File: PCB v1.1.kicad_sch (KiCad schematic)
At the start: 4 parts

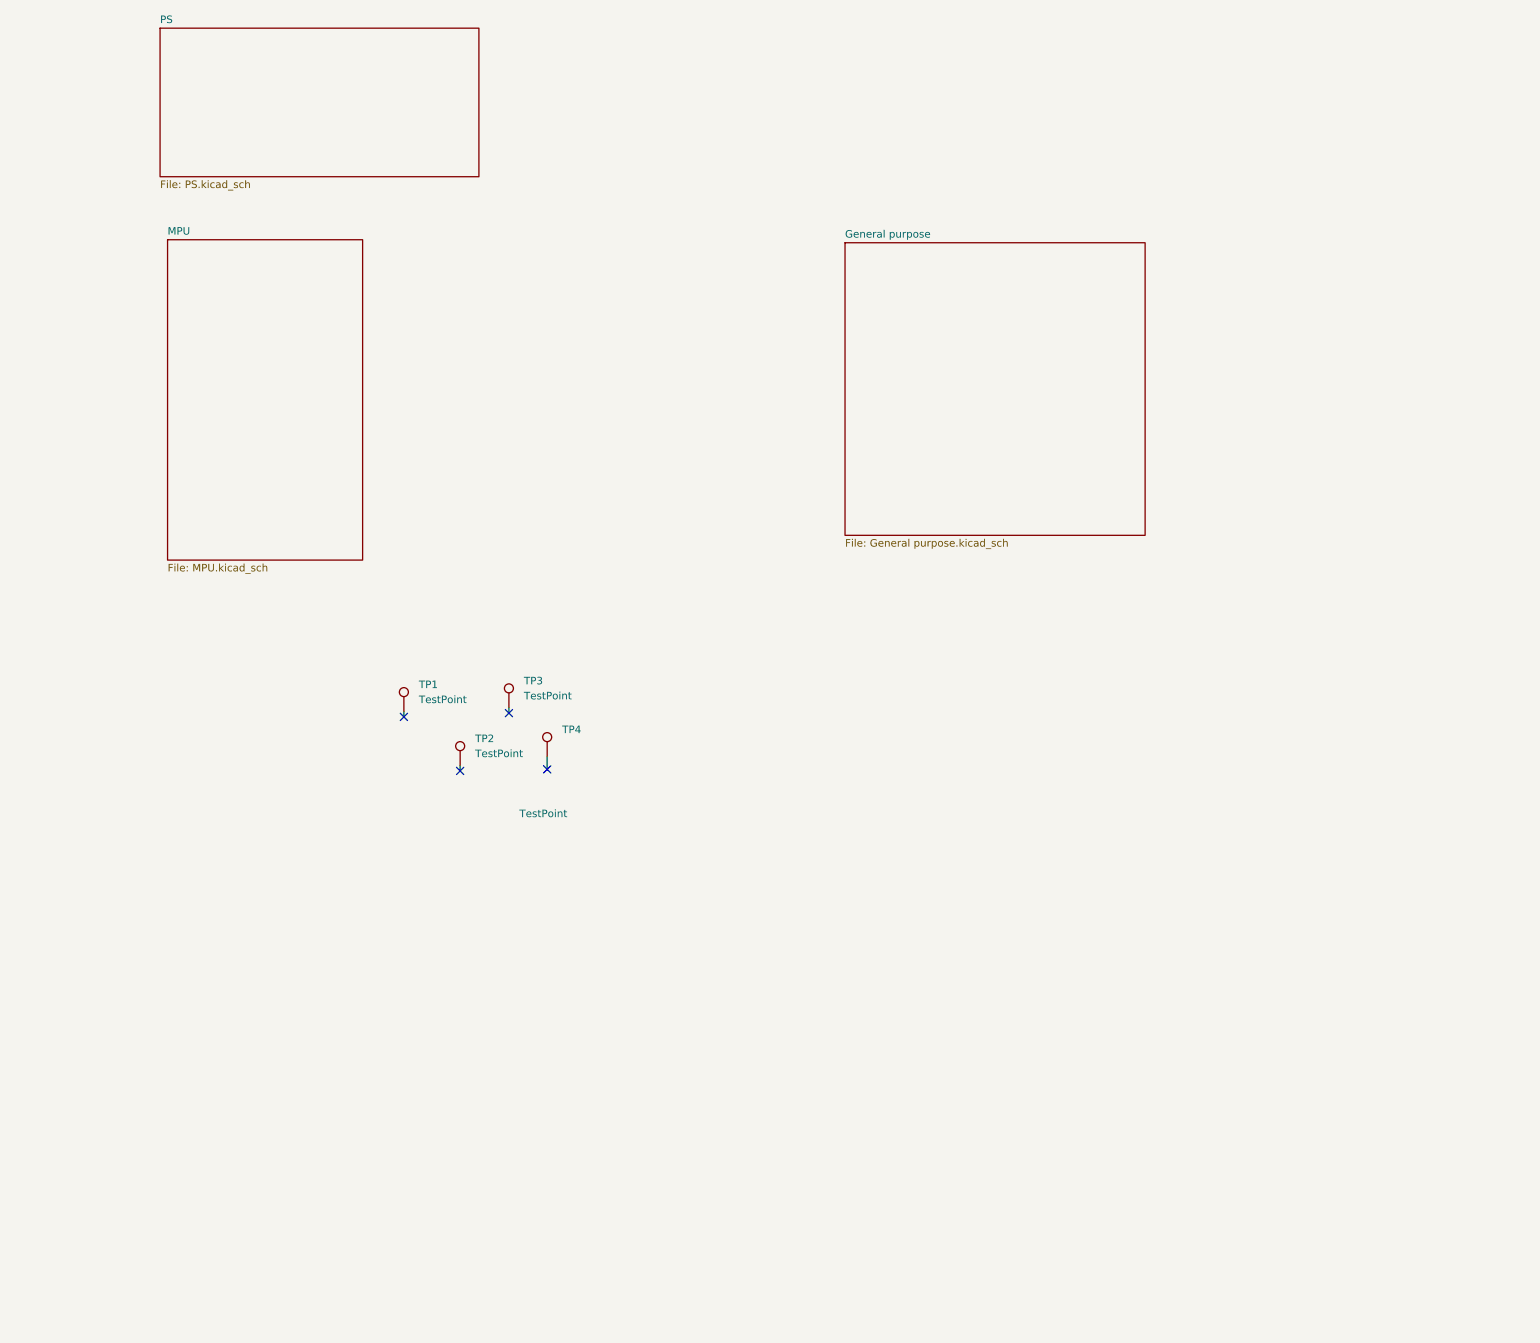
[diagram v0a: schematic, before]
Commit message: schematic tao mot sheet output
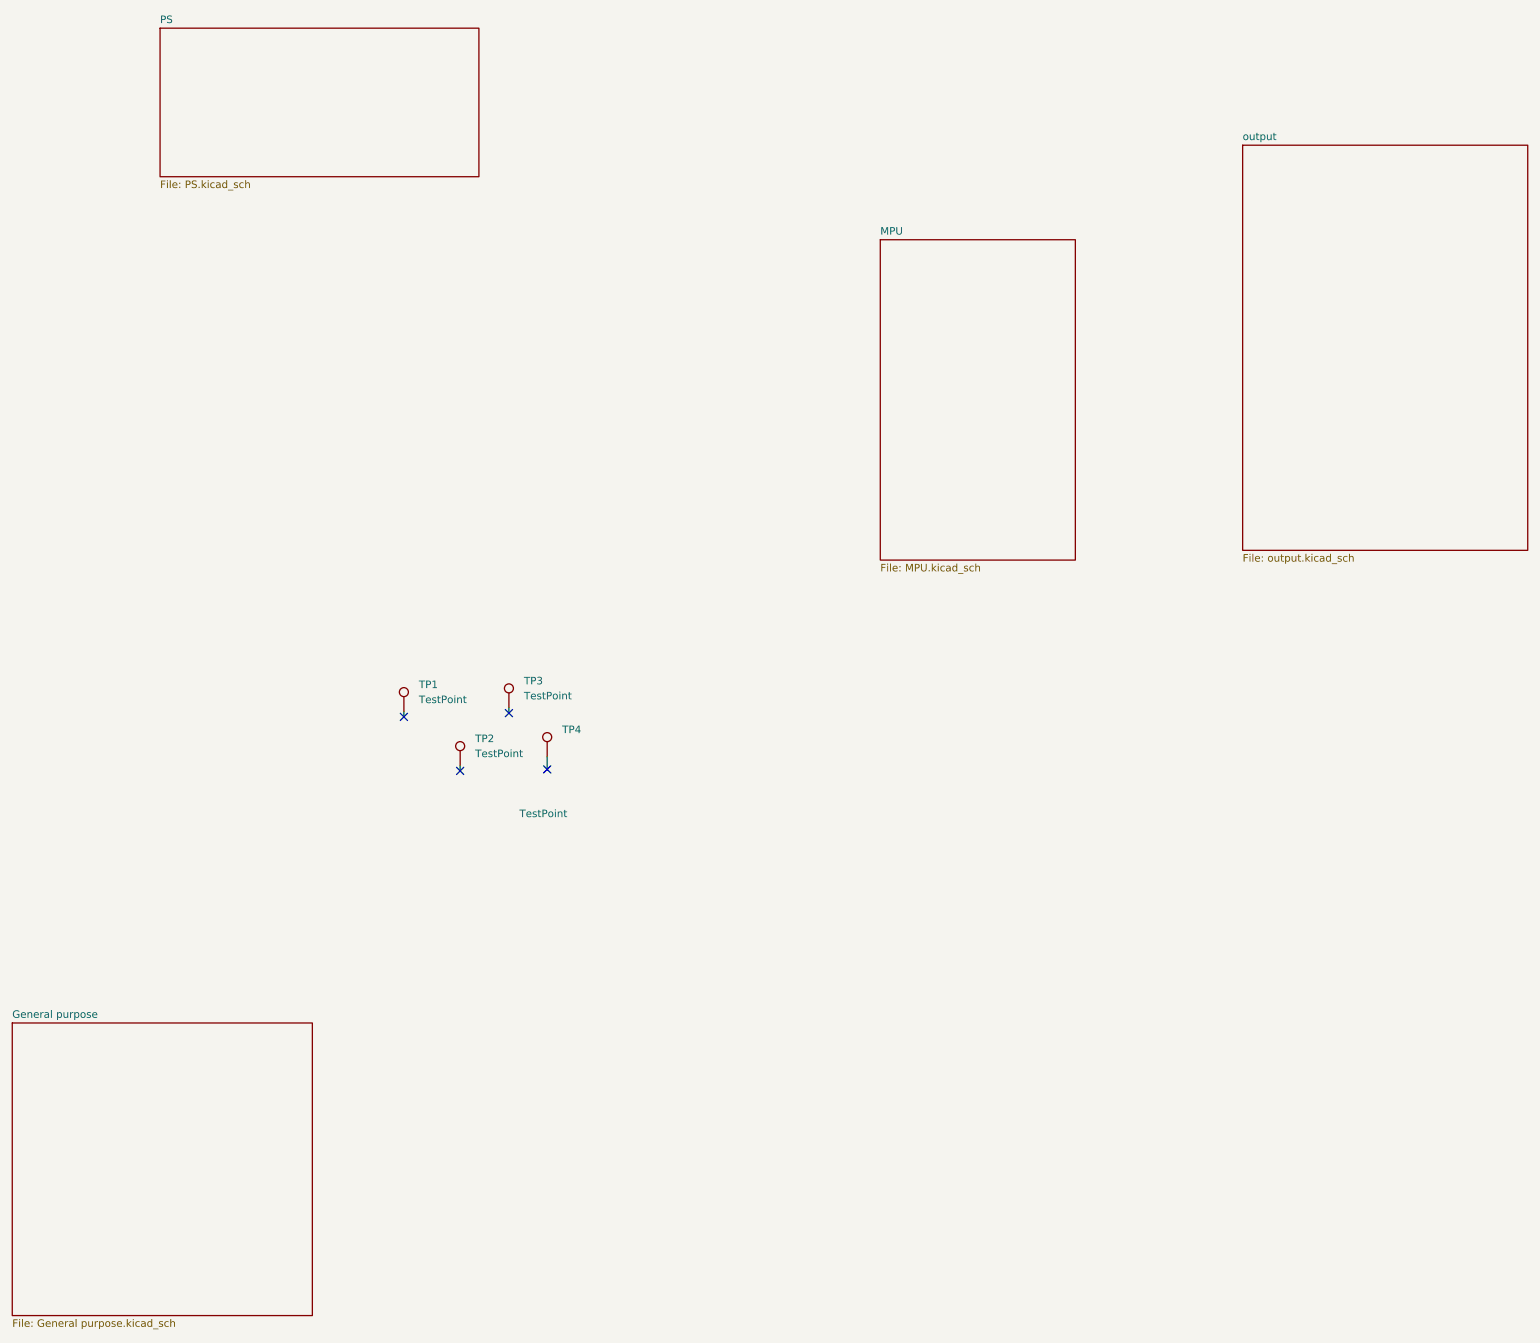
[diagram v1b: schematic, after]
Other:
- added sheet output (output.kicad_sch)
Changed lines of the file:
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@@
 	)
 	(sheet
-		(at 149.86 83.82)
+		(at 8.89 215.9)
 		(size 50.8 49.53)
 		(exclude_from_sim no)
@@
 		)
 		(property "Sheetname" "General purpose"
-			(at 149.86 83.1084 0)
+			(at 8.89 215.1884 0)
 			(show_name no)
 			(do_not_autoplace no)
@@
 		)
 		(property "Sheetfile" "General purpose.kicad_sch"
-			(at 149.86 133.9346 0)
+			(at 8.89 266.0146 0)
 			(show_name no)
 			(do_not_autoplace no)
@@
 	)
 	(sheet
-		(at 35.179 83.312)
+		(at 217.17 67.31)
+		(size 48.26 68.58)
+		(exclude_from_sim no)
+		(in_bom yes)
+		(on_board yes)
+		(dnp no)
+		(fields_autoplaced yes)
+		(stroke
+			(width 0.1524)
+			(type solid)
+		)
+		(fill
+			(color 0 0 0 0)
+		)
+		(property "Sheetname" "output"
+			(at 217.17 66.5984 0)
+			(show_name no)
+			(do_not_autoplace no)
+			(effects
+				(font
+					(size 1.27 1.27)
+				)
+				(justify left bottom)
+			)
+		)
+		(property "Sheetfile" "output.kicad_sch"
+			(at 217.17 136.4746 0)
+			(show_name no)
+			(do_not_autoplace no)
+			(effects
+				(font
+					(size 1.27 1.27)
+				)
+				(justify left top)
+			)
+		)
+		(instances
+			(project "PCB v1.1"
+				(path "/e63e39d7-6ac0-4ffd-8aa3-1841a4541b55"
+					(page "5")
+				)
+			)
+		)
+	)
+	(sheet
+		(at 155.829 83.312)
 		(size 33.02 54.229)
 		(exclude_from_sim no)
@@
 		)
 		(property "Sheetname" "MPU"
-			(at 35.179 82.6004 0)
+			(at 155.829 82.6004 0)
 			(show_name no)
 			(do_not_autoplace no)
@@
 		)
 		(property "Sheetfile" "MPU.kicad_sch"
-			(at 35.179 138.1256 0)
+			(at 155.829 138.1256 0)
 			(show_name no)
 			(do_not_autoplace no)
